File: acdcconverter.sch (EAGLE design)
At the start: 21 parts

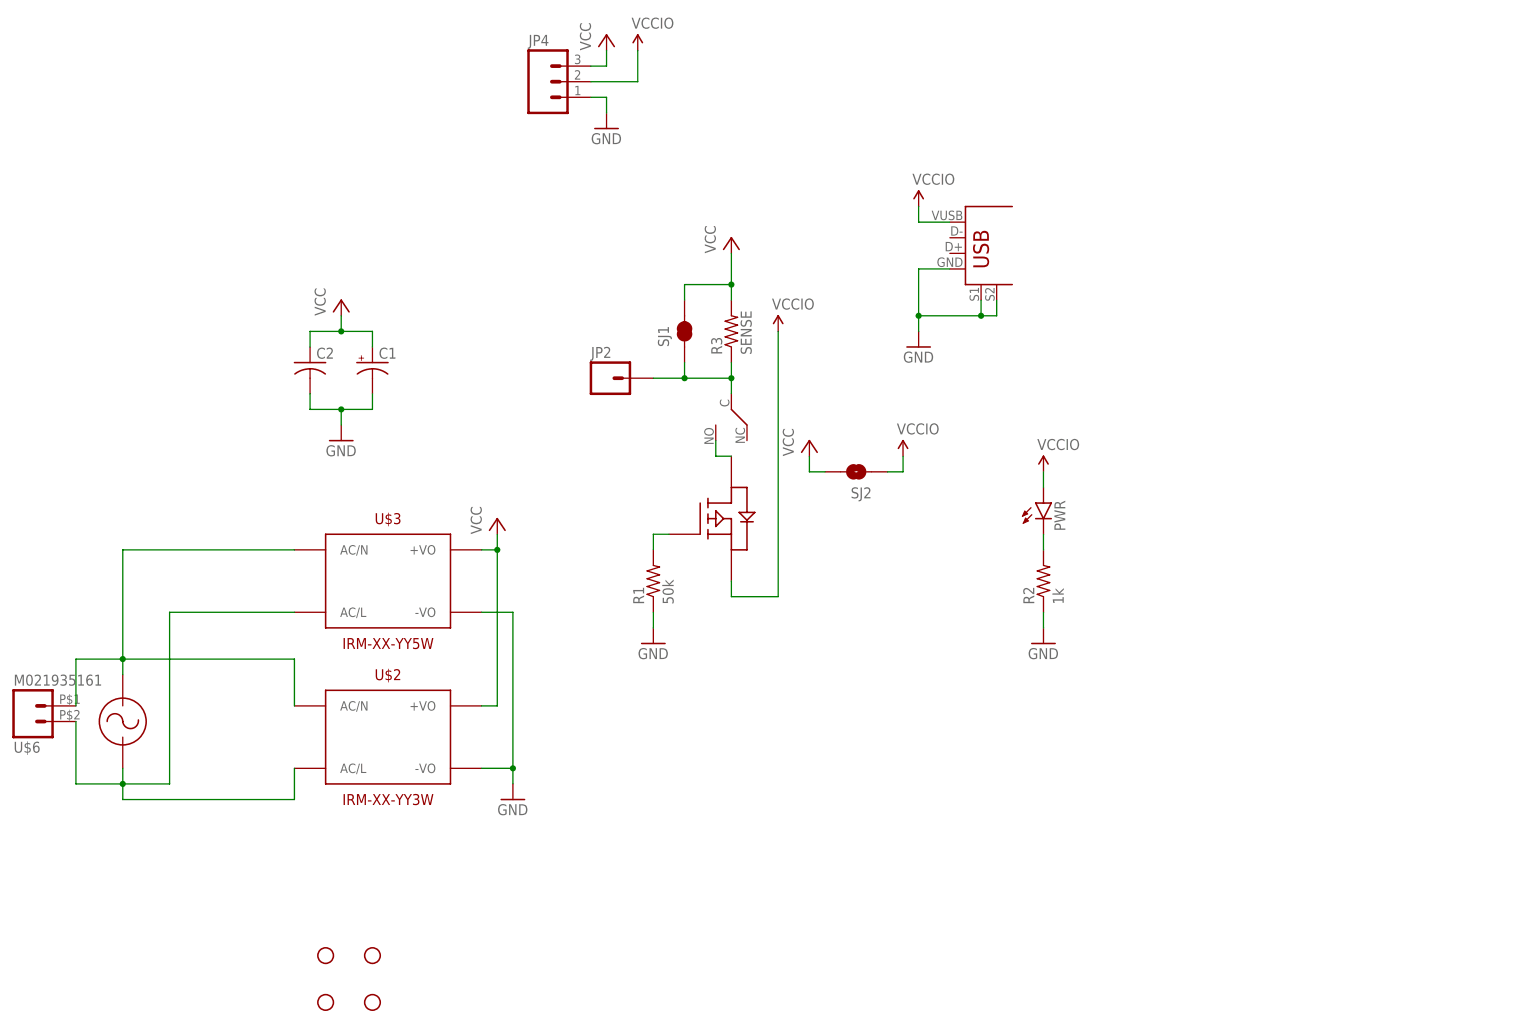
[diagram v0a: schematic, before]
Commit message: Cleaned up the schematic's layout
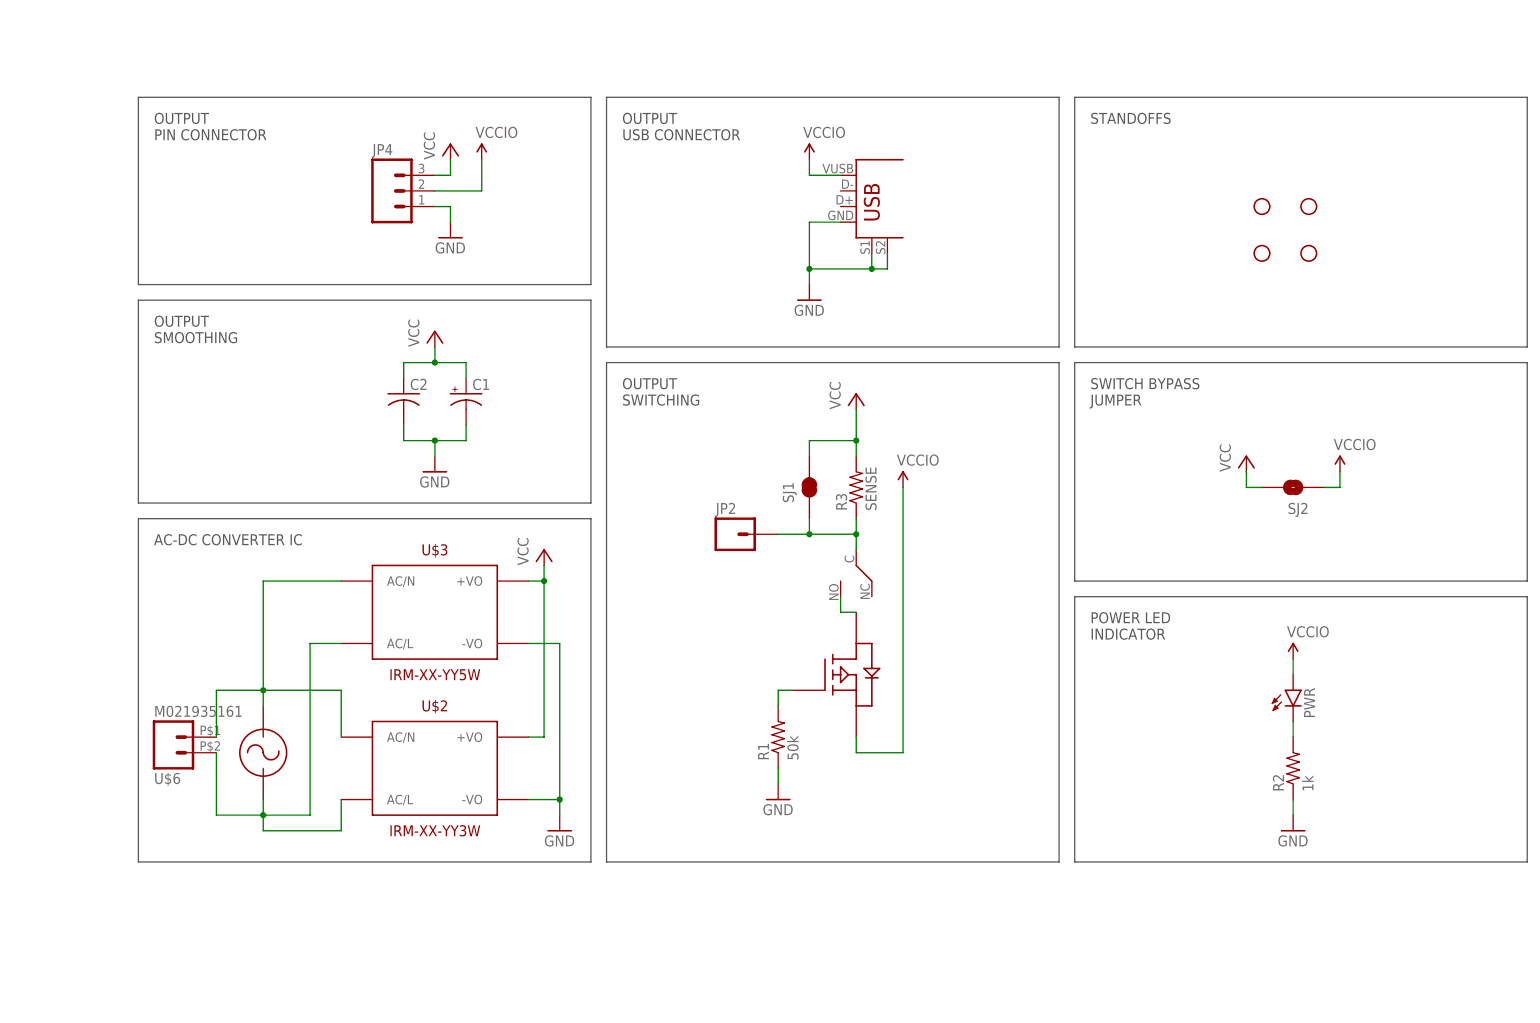
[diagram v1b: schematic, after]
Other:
- note added: "AC-DC CONVERTER IC"
- note added: "OUTPUT PIN CONNECTOR"
- note added: "OUTPUT SMOOTHING"
- note added: "OUTPUT SWITCHING"
- note added: "OUTPUT USB CONNECTOR"
- note added: "POWER LED INDICATOR"
- note added: "STANDOFFS"
- note added: "SWITCH BYPASS JUMPER"
- moved on the sheet: C1, C2, JP2, JP4, PWR, R1, R2, R3, SJ1, SJ2, U$2, U$3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

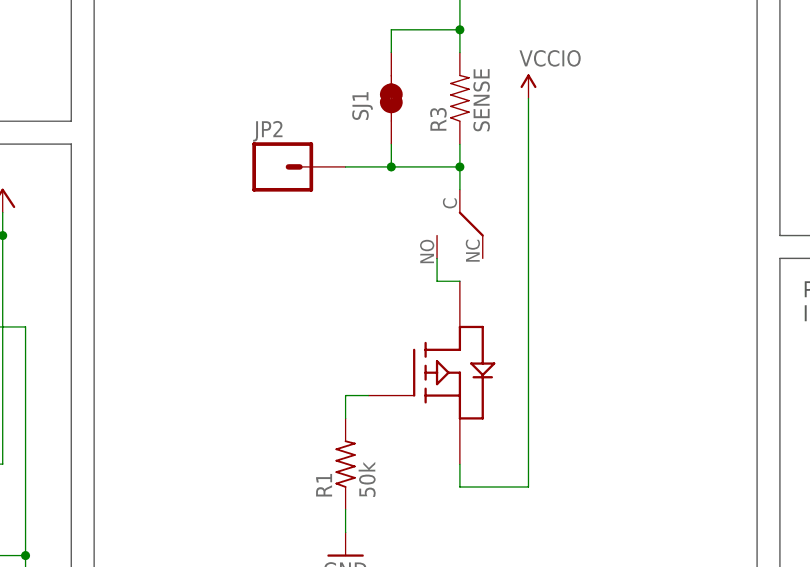
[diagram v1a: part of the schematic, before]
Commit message: Fixed mosfet switch circuit
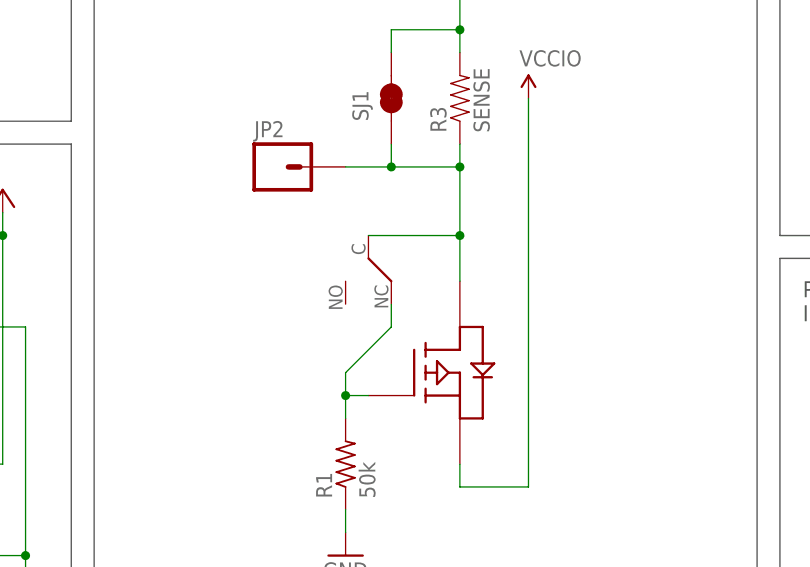
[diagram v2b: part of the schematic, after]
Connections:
- removed net N$5: U$4.DRAIN, U$5.NO
- net N$3: now also U$5.NC
- net N$4: now also U$4.DRAIN
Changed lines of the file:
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@@
 <instance part="R3" gate="G$1" x="116.84" y="60.96" rot="R90"/>
 <instance part="SJ1" gate="G$1" x="109.22" y="60.96" rot="R90"/>
-<instance part="U$5" gate="G$1" x="116.84" y="48.26" rot="R270"/>
+<instance part="U$5" gate="G$1" x="106.68" y="43.18" rot="R270"/>
 <instance part="STANDOFF1" gate="G$1" x="182.88" y="106.68"/>
 <instance part="STANDOFF2" gate="G$1" x="190.5" y="106.68"/>
@@
 <wire x1="104.14" y1="25.4" x2="104.14" y2="27.94" width="0.1524" layer="91"/>
 <wire x1="104.14" y1="27.94" x2="106.68" y2="27.94" width="0.1524" layer="91"/>
+<pinref part="U$5" gate="G$1" pin="NC"/>
+<wire x1="109.22" y1="38.1" x2="109.22" y2="35.56" width="0.1524" layer="91"/>
+<wire x1="109.22" y1="35.56" x2="104.14" y2="30.48" width="0.1524" layer="91"/>
+<wire x1="104.14" y1="30.48" x2="104.14" y2="27.94" width="0.1524" layer="91"/>
+<junction x="104.14" y="27.94"/>
 </segment>
 </net>
@@
 <wire x1="116.84" y1="53.34" x2="109.22" y2="53.34" width="0.1524" layer="91"/>
 <wire x1="109.22" y1="53.34" x2="109.22" y2="55.88" width="0.1524" layer="91"/>
-<pinref part="U$5" gate="G$1" pin="C"/>
-<wire x1="116.84" y1="53.34" x2="116.84" y2="50.8" width="0.1524" layer="91"/>
-<junction x="116.84" y="53.34"/>
 <pinref part="JP2" gate="G$1" pin="1"/>
 <wire x1="104.14" y1="53.34" x2="109.22" y2="53.34" width="0.1524" layer="91"/>
 <junction x="109.22" y="53.34"/>
-</segment>
-</net>
-<net name="N$5" class="0">
-<segment>
-<pinref part="U$5" gate="G$1" pin="NO"/>
 <pinref part="U$4" gate="G$1" pin="DRAIN"/>
-<wire x1="114.3" y1="43.18" x2="114.3" y2="40.64" width="0.1524" layer="91"/>
-<wire x1="114.3" y1="40.64" x2="116.84" y2="40.64" width="0.1524" layer="91"/>
-</segment>
-</net>
+<wire x1="116.84" y1="53.34" x2="116.84" y2="45.72" width="0.1524" layer="91"/>
+<pinref part="U$5" gate="G$1" pin="C"/>
+<wire x1="116.84" y1="45.72" x2="116.84" y2="40.64" width="0.1524" layer="91"/>
+<wire x1="106.68" y1="45.72" x2="116.84" y2="45.72" width="0.1524" layer="91"/>
+<junction x="116.84" y="45.72"/>
+<junction x="116.84" y="53.34"/>
+</segment>
+</net>

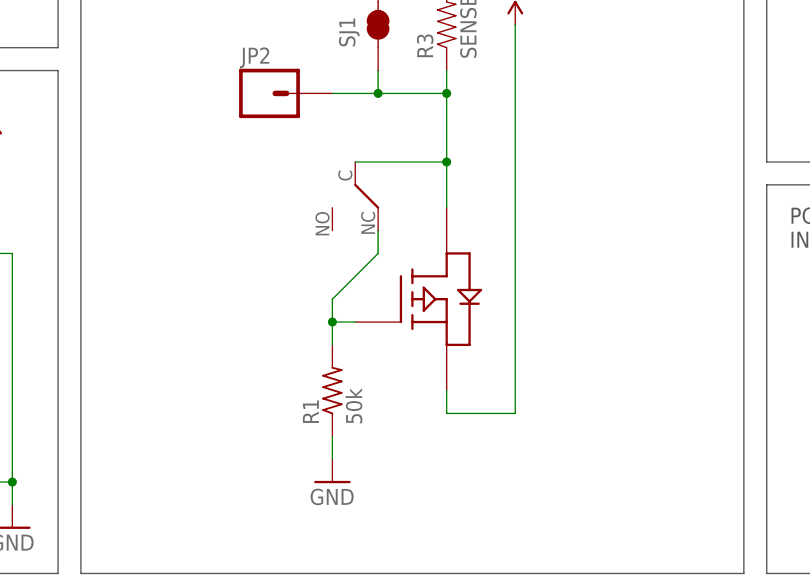
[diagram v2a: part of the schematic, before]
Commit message: Updated MOSFET again
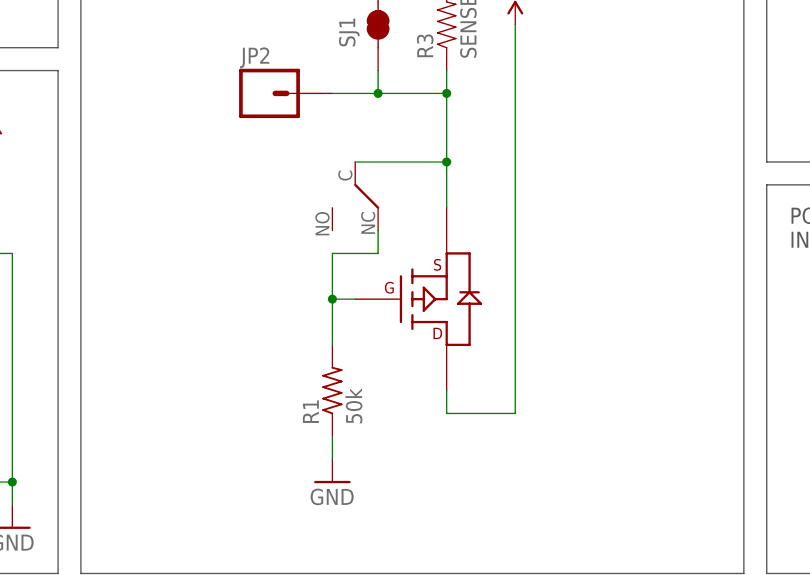
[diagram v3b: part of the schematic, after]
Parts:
- removed U$4: DMG2305UXDMG2305UX, HHJ:DMG2305UXDMG2305UX
- added U$8: MOSFET-PDMG2305UX, HHJ:MOSFET-PDMG2305UX
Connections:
- net N$3: now also U$8.GATE; no longer U$4.GATE
- net N$4: now also U$8.SOURCE; no longer U$4.DRAIN
- net VCCIO: now also U$8.DRAIN; no longer U$4.SOURCE
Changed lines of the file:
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@@
 <part name="C2" library="rcl" deviceset="C-US" device="C0603"/>
 <part name="R1" library="resistor" deviceset="R-US_" device="R0603" value="50k"/>
-<part name="U$4" library="HHJ" deviceset="DMG2305UX" device="DMG2305UX"/>
 <part name="GND1" library="supply1" deviceset="GND" device=""/>
 <part name="P+1" library="supply1" deviceset="VCC" device=""/>
@@
 <part name="SUPPLY5" library="SparkFun-Aesthetics" deviceset="VCCIO" device=""/>
 <part name="GND6" library="supply1" deviceset="GND" device=""/>
+<part name="U$8" library="HHJ" deviceset="MOSFET-P" device="DMG2305UX"/>
 </parts>
 <sheets>
@@
 <instance part="C2" gate="G$1" x="43.18" y="76.2"/>
 <instance part="R1" gate="G$1" x="104.14" y="20.32" rot="R90"/>
-<instance part="U$4" gate="G$1" x="116.84" y="30.48"/>
 <instance part="GND1" gate="1" x="68.58" y="5.08"/>
 <instance part="P+1" gate="VCC" x="66.04" y="50.8"/>
@@
 <instance part="SUPPLY5" gate="G$1" x="109.22" y="114.3"/>
 <instance part="GND6" gate="1" x="109.22" y="91.44"/>
+<instance part="U$8" gate="G$1" x="116.84" y="30.48"/>
 </instances>
 <busses>
@@
 <segment>
 <pinref part="R1" gate="G$1" pin="2"/>
-<pinref part="U$4" gate="G$1" pin="GATE"/>
-<wire x1="104.14" y1="25.4" x2="104.14" y2="27.94" width="0.1524" layer="91"/>
-<wire x1="104.14" y1="27.94" x2="106.68" y2="27.94" width="0.1524" layer="91"/>
+<wire x1="104.14" y1="25.4" x2="104.14" y2="30.48" width="0.1524" layer="91"/>
+<wire x1="104.14" y1="30.48" x2="106.68" y2="30.48" width="0.1524" layer="91"/>
 <pinref part="U$5" gate="G$1" pin="NC"/>
 <wire x1="109.22" y1="38.1" x2="109.22" y2="35.56" width="0.1524" layer="91"/>
-<wire x1="109.22" y1="35.56" x2="104.14" y2="30.48" width="0.1524" layer="91"/>
-<wire x1="104.14" y1="30.48" x2="104.14" y2="27.94" width="0.1524" layer="91"/>
-<junction x="104.14" y="27.94"/>
+<wire x1="109.22" y1="35.56" x2="104.14" y2="35.56" width="0.1524" layer="91"/>
+<wire x1="104.14" y1="35.56" x2="104.14" y2="30.48" width="0.1524" layer="91"/>
+<junction x="104.14" y="30.48"/>
+<pinref part="U$8" gate="G$1" pin="GATE"/>
 </segment>
 </net>
 <net name="VCCIO" class="0">
 <segment>
-<pinref part="U$4" gate="G$1" pin="SOURCE"/>
-<wire x1="116.84" y1="20.32" x2="116.84" y2="17.78" width="0.1524" layer="91"/>
 <pinref part="SUPPLY1" gate="G$1" pin="VCCIO"/>
 <wire x1="116.84" y1="17.78" x2="124.46" y2="17.78" width="0.1524" layer="91"/>
 <wire x1="124.46" y1="17.78" x2="124.46" y2="60.96" width="0.1524" layer="91"/>
+<pinref part="U$8" gate="G$1" pin="DRAIN"/>
+<wire x1="116.84" y1="17.78" x2="116.84" y2="20.32" width="0.1524" layer="91"/>
 </segment>
 <segment>
@@
 <wire x1="104.14" y1="53.34" x2="109.22" y2="53.34" width="0.1524" layer="91"/>
 <junction x="109.22" y="53.34"/>
-<pinref part="U$4" gate="G$1" pin="DRAIN"/>
 <wire x1="116.84" y1="53.34" x2="116.84" y2="45.72" width="0.1524" layer="91"/>
 <pinref part="U$5" gate="G$1" pin="C"/>
-<wire x1="116.84" y1="45.72" x2="116.84" y2="40.64" width="0.1524" layer="91"/>
 <wire x1="106.68" y1="45.72" x2="116.84" y2="45.72" width="0.1524" layer="91"/>
+<junction x="116.84" y="53.34"/>
+<pinref part="U$8" gate="G$1" pin="SOURCE"/>
+<wire x1="116.84" y1="40.64" x2="116.84" y2="45.72" width="0.1524" layer="91"/>
 <junction x="116.84" y="45.72"/>
-<junction x="116.84" y="53.34"/>
-</segment>
-</net>
+</segment>
+</net>
